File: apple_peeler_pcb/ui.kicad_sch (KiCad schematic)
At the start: 8 parts, among them SW3 SPST BTN

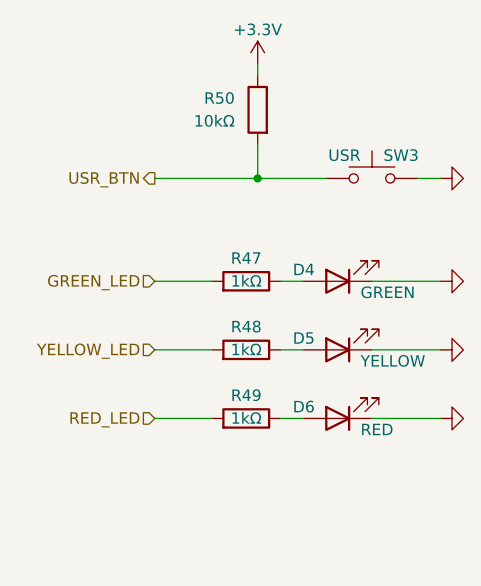
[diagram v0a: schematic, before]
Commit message: add power led
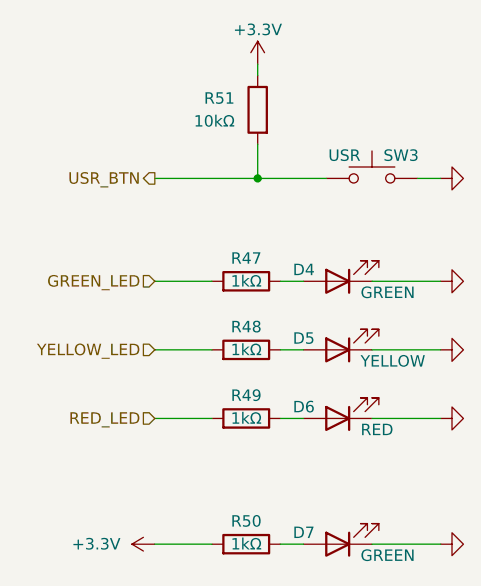
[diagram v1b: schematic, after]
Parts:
- added D7: GREEN, LED_SMD:LED_0805_2012Metric, symbol Device:LED
- added R50: 1kΩ, Resistor_SMD:R_0805_2012Metric, symbol Device:R
- renumbered R50 to R51
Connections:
- net +3.3V: now also R50.2
- net GND: now also D7.1 (K)
- new net: D7.2 (A), R50.1

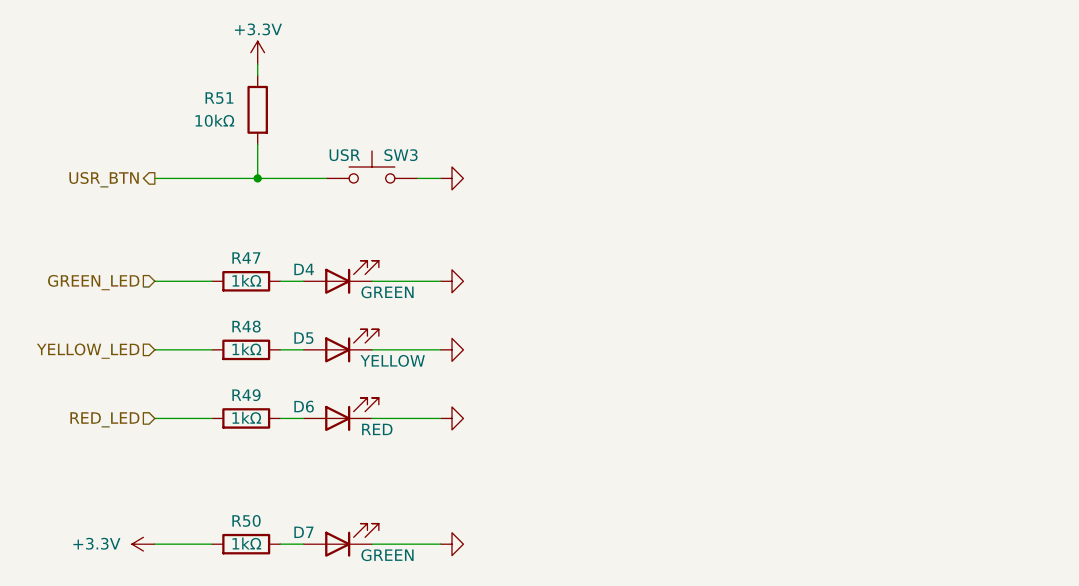
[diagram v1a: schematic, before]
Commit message: use wleds instead of individual leds
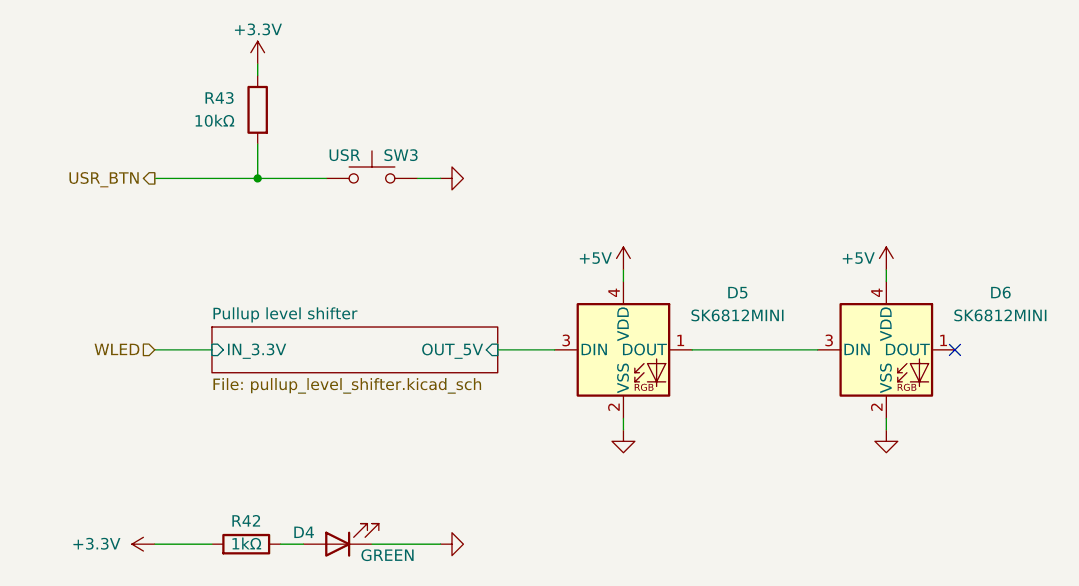
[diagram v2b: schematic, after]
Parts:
- removed D4: GREEN, LED_SMD:LED_0805_2012Metric, symbol Device:LED
- removed D5: YELLOW, LED_SMD:LED_0805_2012Metric, symbol Device:LED
- removed D6: RED, LED_SMD:LED_0805_2012Metric, symbol Device:LED
- removed R47, R48, R49: 1kΩ, Resistor_SMD:R_0805_2012Metric, symbol Device:R
- added D5, D6: SK6812MINI, LED_SMD:LED_SK6812MINI_PLCC4_3.5x3.5mm_P1.75mm, symbol LED:SK6812MINI
- renumbered D7 to D4, R50 to R42, R51 to R43
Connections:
- net GND: now also D5.2 (VSS), D6.2 (VSS)
- new net: D5.1 (DOUT), D6.3 (DIN)
- new net +5V: D5.4 (VDD), D6.4 (VDD)
- new net Pullup level shifter/OUT_5V: D5.3 (DIN)
- no-connect marks 0 -> 1
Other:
- added sheet Pullup level shifter (pullup_level_shifter.kicad_sch)
